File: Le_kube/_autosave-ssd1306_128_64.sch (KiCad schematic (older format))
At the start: 15 parts

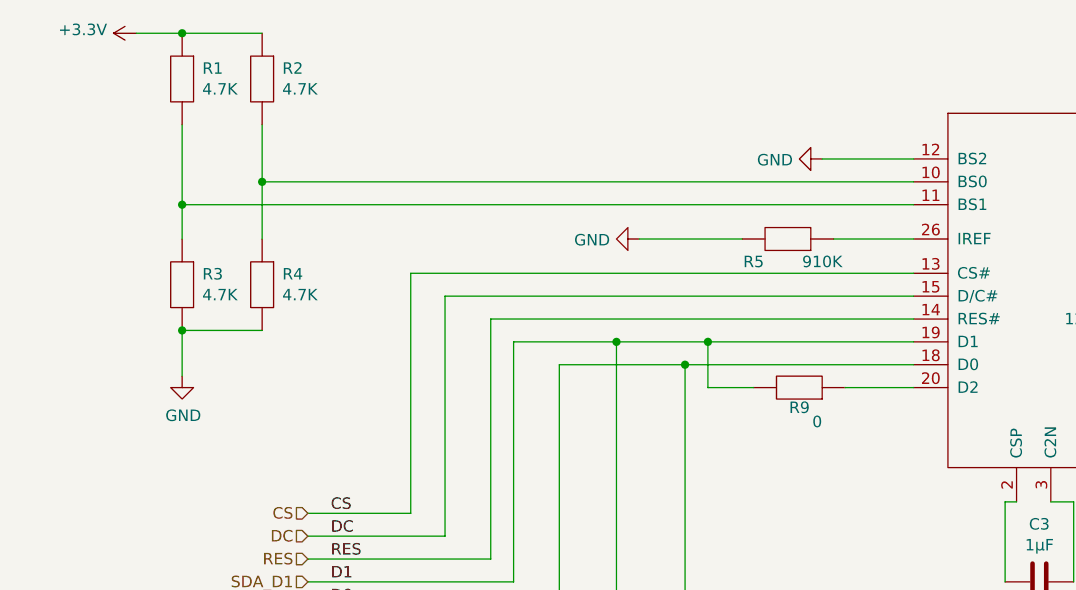
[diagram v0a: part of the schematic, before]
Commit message: screen done
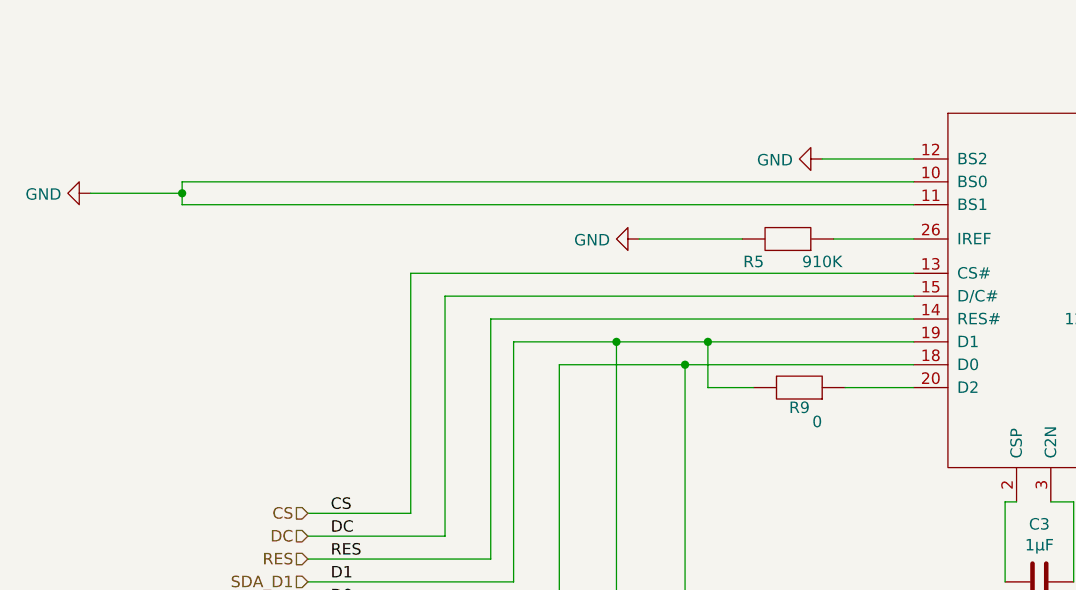
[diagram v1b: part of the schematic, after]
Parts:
- removed R1, R2, R3, R4: 4.7K, symbol Kube_library:R
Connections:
- net GND: now also U.10 (BS0), U.11 (BS1)
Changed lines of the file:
@@
 Comment4 ""
 $EndDescr
-$Comp
-L Kube_library:R R1
-U 1 1 606D3DEF
-P 2400 1350
-F 0 "R1" V 2354 1438 50  0000 L CNN
-F 1 "4.7K" V 2445 1438 50  0000 L CNN
-F 2 "" H 2400 1350 50  0001 C CNN
-F 3 "" H 2400 1350 50  0001 C CNN
-	1    2400 1350
-	0    1    1    0
-$EndComp
-$Comp
-L Kube_library:R R2
-U 1 1 606D4491
-P 2750 1350
-F 0 "R2" V 2704 1438 50  0000 L CNN
-F 1 "4.7K" V 2795 1438 50  0000 L CNN
-F 2 "" H 2750 1350 50  0001 C CNN
-F 3 "" H 2750 1350 50  0001 C CNN
-	1    2750 1350
-	0    1    1    0
-$EndComp
-Wire Wire Line
-	2750 1150 2400 1150
-Connection ~ 2400 1150
-Wire Wire Line
-	2400 1150 2200 1150
-$Comp
-L Kube_library:R R4
-U 1 1 606D4D1A
-P 2750 2250
-F 0 "R4" V 2704 2338 50  0000 L CNN
-F 1 "4.7K" V 2795 2338 50  0000 L CNN
-F 2 "" H 2750 2250 50  0001 C CNN
-F 3 "" H 2750 2250 50  0001 C CNN
-	1    2750 2250
-	0    1    1    0
-$EndComp
-$Comp
-L Kube_library:R R3
-U 1 1 606D54AA
-P 2400 2250
-F 0 "R3" V 2354 2338 50  0000 L CNN
-F 1 "4.7K" V 2445 2338 50  0000 L CNN
-F 2 "" H 2400 2250 50  0001 C CNN
-F 3 "" H 2400 2250 50  0001 C CNN
-	1    2400 2250
-	0    1    1    0
-$EndComp
-Wire Wire Line
-	2400 1550 2400 1900
-Wire Wire Line
-	2750 1550 2750 1800
-Connection ~ 2400 1900
-Wire Wire Line
-	2400 1900 2400 2050
-Connection ~ 2750 1800
-Wire Wire Line
-	2750 1800 2750 2050
-Wire Wire Line
-	2400 2450 2750 2450
-Wire Wire Line
-	2400 2450 2400 2650
-Connection ~ 2400 2450
-$Comp
-L power:GND #PWR?
-U 1 1 606D6329
-P 2400 2650
-F 0 "#PWR?" H 2400 2400 50  0001 C CNN
-F 1 "GND" H 2405 2477 50  0000 C CNN
-F 2 "" H 2400 2650 50  0001 C CNN
-F 3 "" H 2400 2650 50  0001 C CNN
-	1    2400 2650
-	1    0    0    -1
-$EndComp
 Wire Wire Line
 	5600 1700 5200 1700
@@
 	3750 2400 5600 2400
 Wire Wire Line
-	5600 2500 4700 2500
-Wire Wire Line
 	3850 2500 3850 3550
 Wire Wire Line
@@
 Wire Wire Line
 	4050 3650 4050 2600
-Wire Wire Line
-	5600 2700 5300 2700
-$Comp
-L Kube_library:R R9
-U 1 1 60712FDF
-P 5100 2700
-F 0 "R9" H 5054 2788 50  0000 L CNN
-F 1 "0" H 5000 2850 50  0000 L CNN
-F 2 "" H 5100 2700 50  0001 C CNN
-F 3 "" H 5100 2700 50  0001 C CNN
-	1    5100 2700
-	-1   0    0    1
-$EndComp
-Wire Wire Line
-	4900 2700 4700 2700
-Wire Wire Line
-	4700 2700 4700 2500
-Connection ~ 4700 2500
-Wire Wire Line
-	2750 1800 5600 1800
-Wire Wire Line
-	2400 1900 5600 1900
 Wire Wire Line
 	7900 2650 8500 2650
@@
 Wire Wire Line
 	6700 3200 6800 3200
-$Comp
-L power:+3.3V #PWR?
-U 1 1 607E436B
-P 2200 1150
-F 0 "#PWR?" H 2200 1000 50  0001 C CNN
-F 1 "+3.3V" V 2215 1278 50  0000 L CNN
-F 2 "" H 2200 1150 50  0001 C CNN
-F 3 "" H 2200 1150 50  0001 C CNN
-	1    2200 1150
-	0    -1   -1   0
-$EndComp
 Text HLabel 2950 3250 0    50   Input ~ 0
 CS
@@
 Wire Wire Line
 	4300 2500 3850 2500
-Wire Wire Line
-	4700 2500 4300 2500
 Connection ~ 4600 2600
 Wire Wire Line
@@
 Wire Wire Line
 	4450 4000 4450 5200
+Wire Wire Line
+	4700 2500 4300 2500
+Wire Wire Line
+	5600 2500 4700 2500
+Connection ~ 4700 2500
+Wire Wire Line
+	4700 2700 4700 2500
+Wire Wire Line
+	4900 2700 4700 2700
+$Comp
+L Kube_library:R R9
+U 1 1 60712FDF
+P 5100 2700
+F 0 "R9" H 5054 2788 50  0000 L CNN
+F 1 "0" H 5000 2850 50  0000 L CNN
+F 2 "" H 5100 2700 50  0001 C CNN
+F 3 "" H 5100 2700 50  0001 C CNN
+	1    5100 2700
+	-1   0    0    1
+$EndComp
+Wire Wire Line
+	5600 2700 5300 2700
+Wire Wire Line
+	2400 1900 5600 1900
+Wire Wire Line
+	2400 1800 2400 1850
+Wire Wire Line
+	2400 1800 5600 1800
+Wire Wire Line
+	2400 1850 2000 1850
+Connection ~ 2400 1850
+Wire Wire Line
+	2400 1850 2400 1900
+$Comp
+L power:GND #PWR?
+U 1 1 60830AF6
+P 2000 1850
+F 0 "#PWR?" H 2000 1600 50  0001 C CNN
+F 1 "GND" V 2005 1722 50  0000 R CNN
+F 2 "" H 2000 1850 50  0001 C CNN
+F 3 "" H 2000 1850 50  0001 C CNN
+	1    2000 1850
+	0    1    1    0
+$EndComp
 $EndSCHEMATC
